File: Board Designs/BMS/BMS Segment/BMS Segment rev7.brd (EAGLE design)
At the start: 110 x 242.3 mm, 273 parts

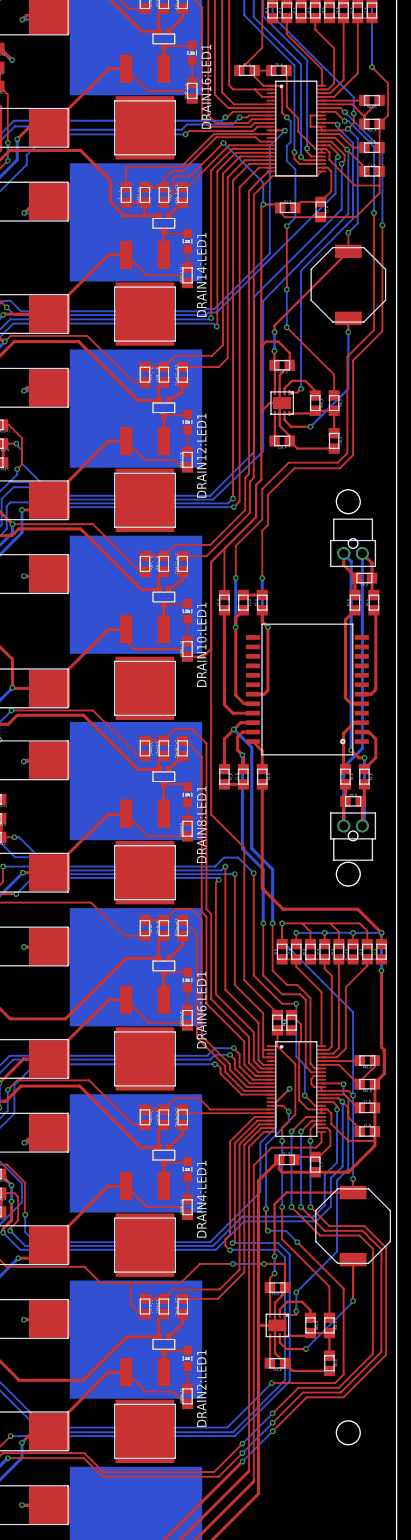
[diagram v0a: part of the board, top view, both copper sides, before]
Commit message: BMS rev7: use NPN regulator instead of buck converter, Front ECU rev6: Use I2C for accelerometer, HV Board rev4: Add shutdown circuit line to BMS ADC, External diagrams for both competitions
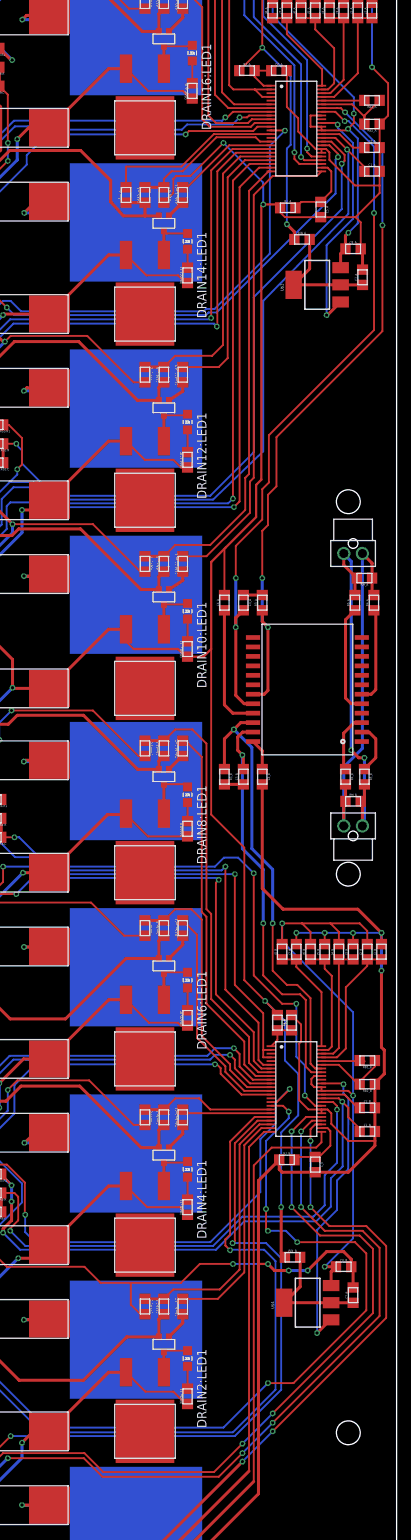
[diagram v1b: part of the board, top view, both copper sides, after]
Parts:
- removed BUCK_CONV_A, BUCK_CONV_B: ADP2360, HyTechDevices:LFCSP-8
- removed CIN_A, CIN_B: 4.7uF, HyTechDevices:0805
- removed COUT_A, COUT_B: 22uF, HyTechDevices:0805
- removed CSS_A, CSS_B: 2.2nF, HyTechDevices:0805
- removed L1_A, L1_B: 330uH, HyTechDevices:SRU1048
- removed RPG_A, RPG_B: 1kΩ, HyTechDevices:0805
- added C7_A, C7_B: 0.1uF, HyTechDevices:0805
- added C8_A, C8_B: 1uF, HyTechDevices:0805
- added U$3, U$4: (no value), HyTechDevices:SOT223
- RIN_A, RIN_B: value 1kΩ -> 100Ω
- moved RIN_A 22.4 mm to (97.3, 181.4), turned to 0 degrees
- moved RIN_B 10.4 mm to (96.0, 44.7), turned to 0 degrees
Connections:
- removed net N$11: BUCK_CONV_B.8, CIN_B.1, RIN_B.2, RPG_B.2
- removed net N$12: BUCK_CONV_B.2, RPG_B.1
- removed net N$14: BUCK_CONV_B.5, CSS_B.2
- removed net N$15: BUCK_CONV_B.7, L1_B.1
- removed net N$25: BUCK_CONV_A.8, CIN_A.1, RIN_A.2, RPG_A.2
- removed net N$27: BUCK_CONV_A.2, RPG_A.1
- removed net N$28: BUCK_CONV_A.5, CSS_A.2
- removed net N$29: BUCK_CONV_A.7, L1_A.1
- new net VIN_A: C7_A.1, RIN_A.2, U$3.2, U$3.4
- new net VIN_B: C7_B.1, RIN_B.2, U$4.2, U$4.4
- net DRIVE_A: now also U$3.1; no longer BUCK_CONV_A.1
- net DRIVE_B: now also U$4.1; no longer BUCK_CONV_B.1
- net SENSE18: now also RIN_A.1
- net V+_A: no longer RIN_A.1
- net V+_B: no longer RIN_B.1
- net V-_A: now also C7_A.2, C8_A.2, RIN_B.1; no longer BUCK_CONV_A.3, BUCK_CONV_A.6, BUCK_CONV_A.PAD, CIN_A.2, COUT_A.1, CSS_A.1
- net V-_B: now also C7_B.2, C8_B.2; no longer BUCK_CONV_B.3, BUCK_CONV_B.6, BUCK_CONV_B.PAD, CIN_B.2, COUT_B.1, CSS_B.1
- net VREG_A: now also C8_A.1, U$3.3; no longer BUCK_CONV_A.4, COUT_A.2, L1_A.2
- net VREG_B: now also C8_B.1, U$4.3; no longer BUCK_CONV_B.4, COUT_B.2, L1_B.2
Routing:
- net V+_A: track 52.9 -> 5.79 mm, vias 4 -> 0
- net V+_B: track 46.1 -> 4.78 mm, vias 2 -> 0
- net SENSE18: track 110.2 -> 138.1 mm, vias 0 -> 2
- net N$29: track 21.4 -> 0.00 mm, vias 2 -> 0
- net VREG_A: track 99.8 -> 79.3 mm, vias 6 -> 4
- net N$15: track 19.4 -> 0.00 mm, vias 2 -> 0
- net V-_A: track 798.6 -> 815.9 mm, vias 23 -> 25
- net VIN_B: track 0.00 -> 16.2 mm
- net VIN_A: track 0.00 -> 16.2 mm
- net VREG_B: track 98.4 -> 87.6 mm, vias 5 -> 3
- net DRIVE_A: track 43.3 -> 32.8 mm
- net N$11: track 9.20 -> 0.00 mm
- net N$25: track 9.20 -> 0.00 mm
- net V-_B: track 736.2 -> 727.7 mm, vias 20 -> 22
- net N$12: track 6.78 -> 0.00 mm
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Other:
- board text added: "HyTech 2018 BMS Segment rev7"
- board text removed: "HyTech 2018 BMS Segment rev6"
